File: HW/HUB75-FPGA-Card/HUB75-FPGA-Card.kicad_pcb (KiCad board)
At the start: 4 copper layers, 53.3 x 85.1 mm, 129 parts, among them J1 Conn_02x04_Odd_Even, J10 USB_C_Receptacle_USB2.0_14P, J11 USB_A, J12 Conn_02x06_Odd_Even, J13 Conn_01x02, J14 Conn_01x02, J16 Conn_01x04, J17 Conn_01x04, J2 Conn_02x08_Odd_Even, J3 Conn_02x08_Odd_Even, J4 Conn_01x01, J5 Conn_01x01, J6 Conn_01x03, J7 Conn_01x03, J8 Conn_01x03, J9 Conn_01x03, Q1 AO3400A, Q2 AO3400A, SW1 SW_Push, U1 AMS1117-3.3, U10 WMM7037AT2, U11 USBLC6-2SC6, U12 CH334R, U13 W25Q128JVS, U14 RP2040, U2 AP2112K-1.2, U3 T20Q100F3, U4 74AHCT245PW, U5 74AHCT245PW, U6 74AHCT245PW, U7 93LCxxBxxOT, U8 FT232H, U9 HS-100B, X1 ECS-2520MV-xxx-xx, Y1 Crystal_GND24

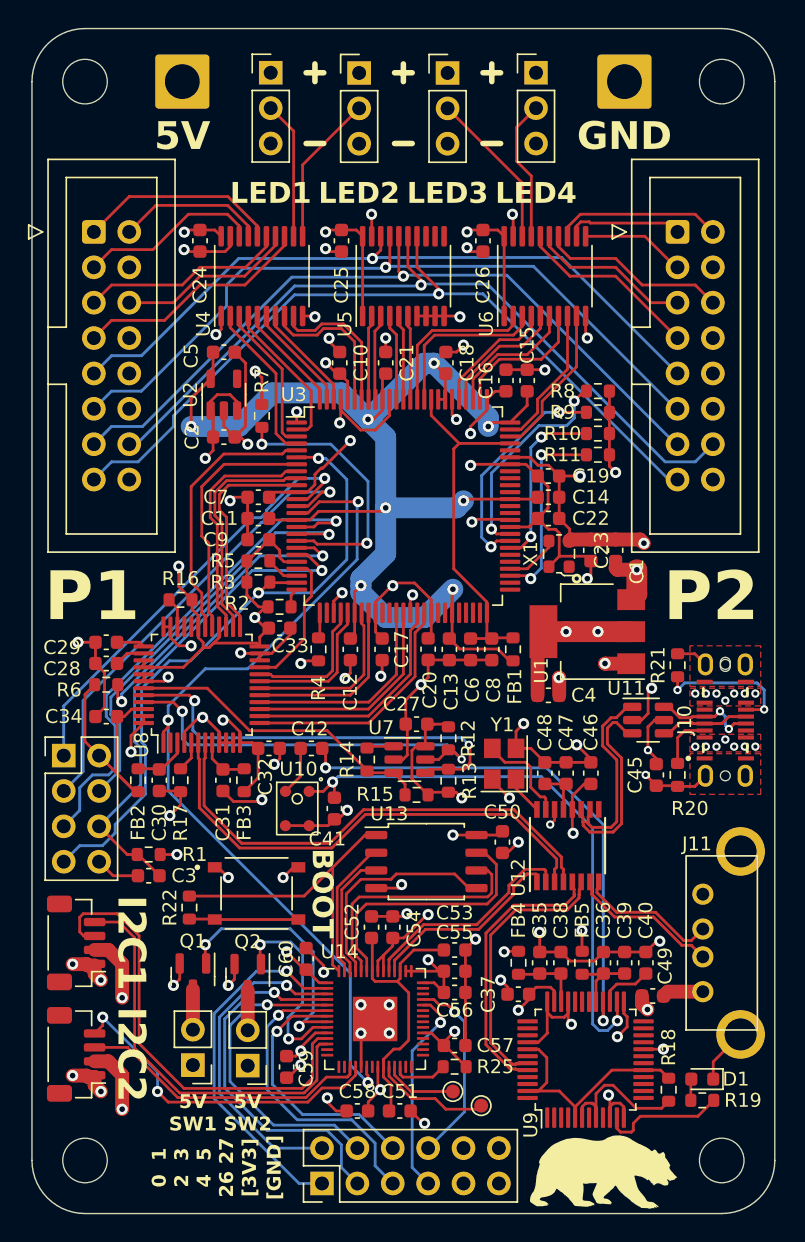
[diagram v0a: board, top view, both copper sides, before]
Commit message: update components and generate production files
still need to look into CBSEL
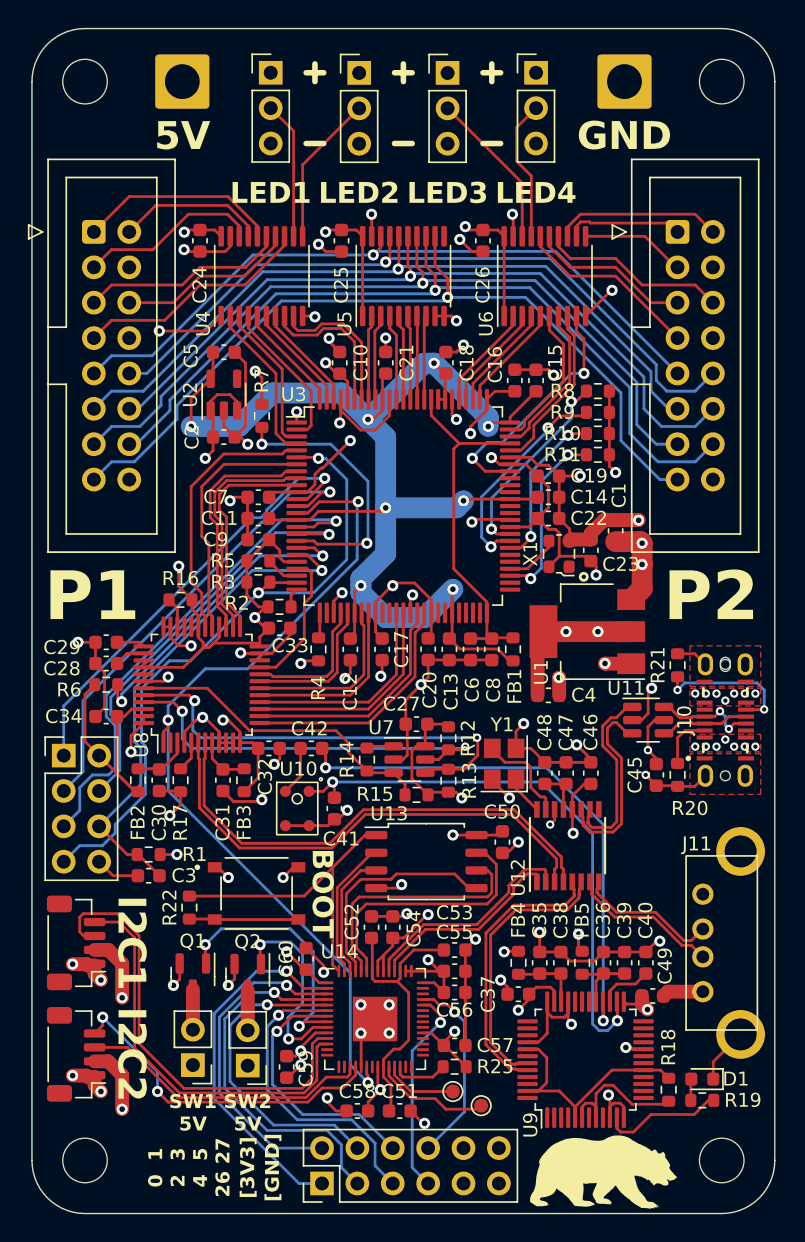
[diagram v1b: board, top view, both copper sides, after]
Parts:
- moved C1 1.40 mm to (129.5, 83.7)
- moved C15 0.64 mm to (123.8, 72.9)
- moved C16 0.64 mm to (122.3, 72.9)
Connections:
- net /FPGA/ROW_CLK renamed /FPGA/A_ROW_CLK
- net /FPGA/ROW_DATA renamed /FPGA/B
- net /Level Shifters/RCLK_out renamed /Level Shifters/A_RCLK_out
- J2 pad 10: GND -> /Level Shifters/B_out
- J2 pad 11: /Level Shifters/RDAT_out -> /Level Shifters/C_RDAT_out
- J2 pad 12: GND -> /Level Shifters/D_out
- J3 pad 10: GND -> /Level Shifters/B_out
- J3 pad 11: /Level Shifters/RDAT_out -> /Level Shifters/C_RDAT_out
- J3 pad 12: GND -> /Level Shifters/D_out
- U3 pad 68: unconnected-(U3C-GPIOR_116_CTRL15-Pad68) -> /FPGA/R3
- U3 pad 71: unconnected-(U3C-GPIOR_94_CDI27-Pad71) -> /FPGA/B3
- U3 pad 73: /FPGA/R3 -> /FPGA/G3
- U3 pad 74: /FPGA/B3 -> /FPGA/G4
- U3 pad 77: /FPGA/G3 -> /FPGA/B4
- U3 pad 78: /FPGA/G4 -> /FPGA/R4
- U3 pad 79: /FPGA/B4 -> /FPGA/STRIP4
- U3 pad 80: /FPGA/R4 -> /FPGA/STRIP3
- U3 pad 85: /FPGA/STRIP4 -> /FPGA/BLANK
- U3 pad 86: /FPGA/STRIP3 -> /FPGA/LAT
- U3 pad 87: /FPGA/BLANK -> /FPGA/CLKOUT
- U3 pad 88: /FPGA/LAT -> /FPGA/D
- U3 pad 89: /FPGA/CLKOUT -> /FPGA/C_ROW_DATA
- U5 pad 12: unconnected-(U5-B6-Pad12) -> /Level Shifters/BLNK_out
- U5 pad 13: unconnected-(U5-B5-Pad13) -> /Level Shifters/LAT_out
- U5 pad 14: /Level Shifters/BLNK_out -> /Level Shifters/CLK_out
- U5 pad 15: /Level Shifters/LAT_out -> /Level Shifters/D_out
- U5 pad 16: /Level Shifters/CLK_out -> /Level Shifters/C_RDAT_out
- U5 pad 17: /Level Shifters/RDAT_out -> /Level Shifters/B_out
- U5 pad 4: /FPGA/CLKOUT -> /FPGA/C_ROW_DATA
- U5 pad 5: /FPGA/LAT -> /FPGA/D
- U5 pad 6: /FPGA/BLANK -> /FPGA/CLKOUT
- U5 pad 7: GND -> /FPGA/LAT
- U5 pad 8: GND -> /FPGA/BLANK
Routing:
- net /Level Shifters/D_out: track 0.00 -> 55.3 mm, vias 0 -> 1
- net /Level Shifters/RDAT_out: track 53.6 -> 0.00 mm, vias 1 -> 0
- net /Level Shifters/C_RDAT_out: track 0.00 -> 53.6 mm, vias 0 -> 1
- net /Level Shifters/B_out: track 0.00 -> 52.4 mm, vias 0 -> 1
- net /FPGA/R3: track 11.1 -> 18.0 mm, vias 0 -> 2
- net /FPGA/C_ROW_DATA: track 0.00 -> 6.19 mm
- net /FPGA/D: track 0.00 -> 6.12 mm
- net +5V: track 44.2 -> 50.0 mm, vias 24 -> 25
- net /FPGA/STRIP4: track 12.2 -> 7.66 mm
- net /FPGA/STRIP3: track 12.0 -> 7.59 mm
- net /Level Shifters/LAT_out: track 57.0 -> 59.4 mm
- net /Level Shifters/CLK_out: track 55.0 -> 57.3 mm
- net /Level Shifters/BLNK_out: track 58.1 -> 60.1 mm
- net /FPGA/B3: track 10.3 -> 12.2 mm
- net /FPGA/B4: track 9.17 -> 7.78 mm
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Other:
- board text added: "SW1 5V"
- board text added: "SW2 5V"
- board text removed: "5V SW1"
- board text removed: "5V SW2"

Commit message: initial design for sbc 5v power board
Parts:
- added JP1: Jumper_2_Open, Connector_PinHeader_2.54mm:PinHeader_1x02_P2.54mm_Vertical, F.Cu at (131.8, 105.8)
- added R23: 10k, Resistor_SMD:R_0603_1608Metric, F.Cu at (137.0, 104.3)
- added R24: 10k, Resistor_SMD:R_0603_1608Metric, F.Cu at (138.6, 104.3)
- moved R18 12.1 mm to (121.3, 124.5)
- moved D1 3.47 mm to (138.8, 124.7)
- moved TP1 1.66 mm to (118.2, 125.1)
- moved J11 1.65 mm to (137.2, 114.9)
- moved TP2 1.40 mm to (116.5, 124.0)
- moved C15 0.51 mm to (123.3, 72.9)
- moved C16 0.51 mm to (121.8, 72.9)
- moved R19 0.28 mm to (135.5, 124.7), turned to 0 degrees
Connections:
- U3 pad 66: unconnected-(U3C-GPIOR_122_CLK13_CDI21-Pad66) -> /FPGA/R3
- U3 pad 67: unconnected-(U3C-GPIOR_117_CTRL14-Pad67) -> /FPGA/B3
- U3 pad 68: /FPGA/R3 -> /FPGA/G3
- U3 pad 71: /FPGA/B3 -> /FPGA/G4
- U3 pad 73: /FPGA/G3 -> /FPGA/B4
- U3 pad 74: /FPGA/G4 -> /FPGA/R4
- U3 pad 77: /FPGA/B4 -> /FPGA/STRIP4
- U3 pad 78: /FPGA/R4 -> /FPGA/STRIP3
- U3 pad 79: /FPGA/STRIP4 -> /FPGA/BLANK
- U3 pad 80: /FPGA/STRIP3 -> /FPGA/LAT
- U3 pad 85: /FPGA/BLANK -> /FPGA/CLKOUT
- U3 pad 86: /FPGA/LAT -> /FPGA/D
- U3 pad 87: /FPGA/CLKOUT -> /FPGA/C_ROW_DATA
- U3 pad 88: /FPGA/D -> /FPGA/B
- U3 pad 89: /FPGA/C_ROW_DATA -> /FPGA/A_ROW_CLK
- U3 pad 92: /FPGA/B -> Net-(JP1-A)
- U3 pad 93: /FPGA/A_ROW_CLK -> Net-(U3B-GPIOL_69_CBSEL1)
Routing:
- net Net-(U3B-GPIOL_69_CBSEL1): track 0.00 -> 48.0 mm, vias 0 -> 2
- net Net-(JP1-A): track 0.00 -> 46.7 mm, vias 0 -> 1
- net +3V3: track 189.0 -> 196.2 mm, vias 26 -> 27
- net /FPGA/B3: track 12.2 -> 18.6 mm, vias 0 -> 2
- net /FPGA/G3: track 11.2 -> 16.8 mm, vias 0 -> 2
- net Net-(U3C-GPIOR_150_CBUS1): track 15.6 -> 20.8 mm
- net /FPGA/LAT: track 6.00 -> 9.35 mm
- net /FPGA/BLANK: track 6.04 -> 9.13 mm
- net /FPGA/B4: track 7.78 -> 10.6 mm
- net /FPGA/R4: track 7.72 -> 9.93 mm
- net Net-(U9-LEDO): track 8.78 -> 6.83 mm
- net Net-(U14-SWCLK): track 8.37 -> 6.56 mm
- net /USB Hub/USB_EXT_D+: track 10.2 -> 11.9 mm
- net /USB Hub/USB_EXT_D-: track 10.8 -> 12.4 mm
- net Net-(U14-SWD): track 5.27 -> 3.87 mm
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
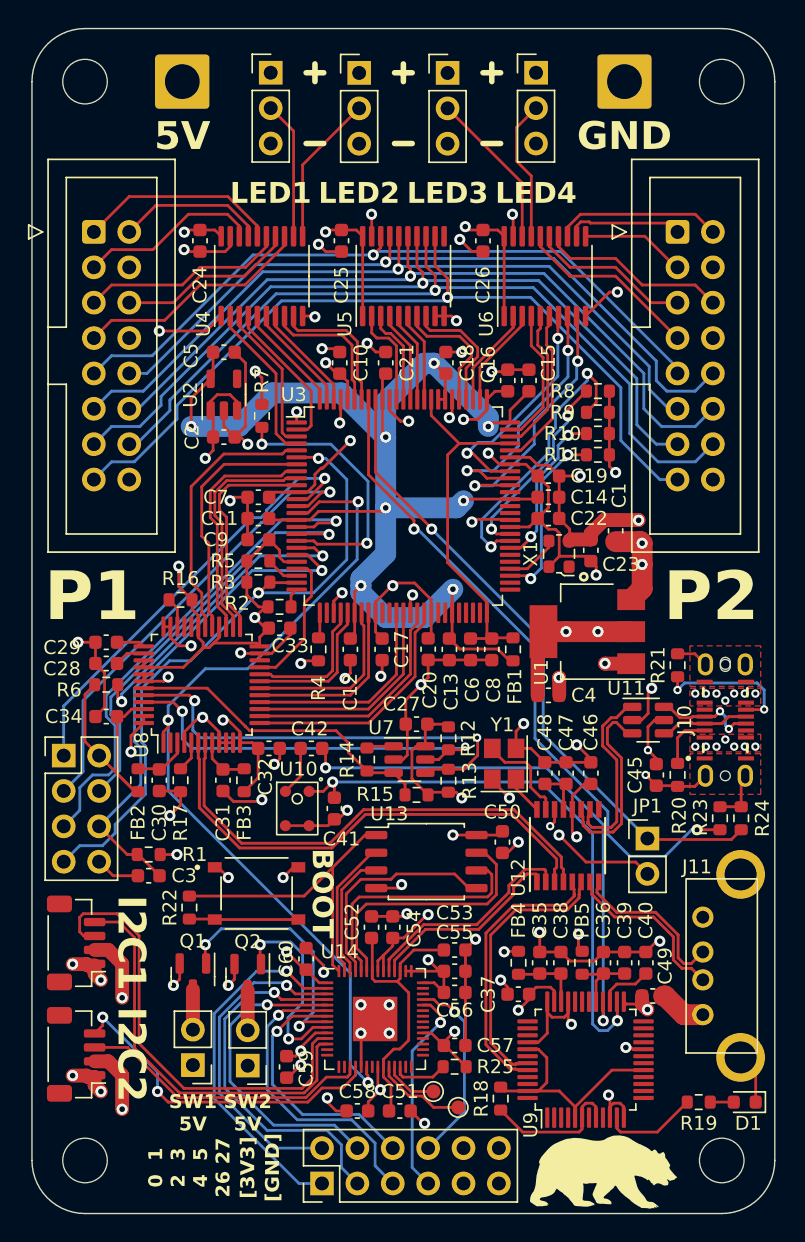
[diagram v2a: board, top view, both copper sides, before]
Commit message: migrate to kicad 8
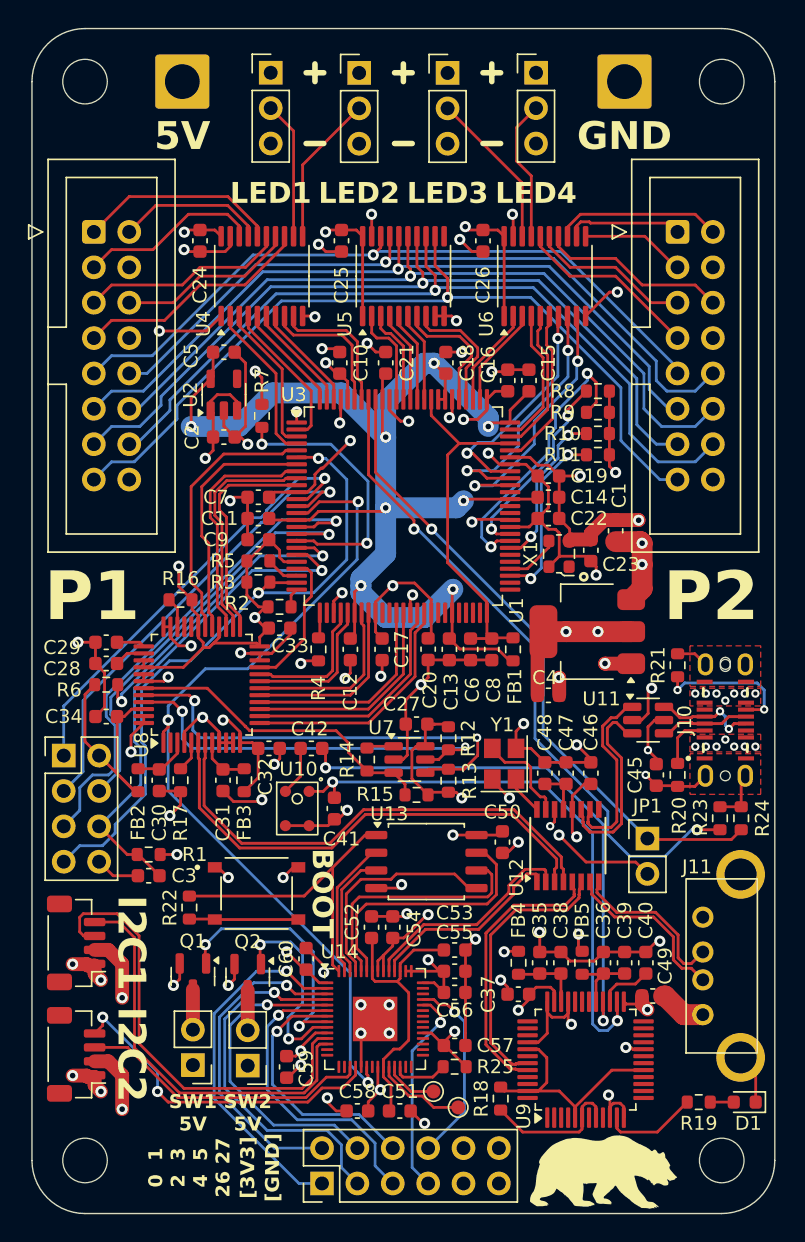
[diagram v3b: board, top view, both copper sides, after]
